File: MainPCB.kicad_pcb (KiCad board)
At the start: 4 copper layers, 105 x 62.4 mm, 41 parts, among them J1 RaspberryPi, J10 Conn_01x02, J2 Conn_01x03, J3 Screw_Terminal_01x02, J4 Conn_01x02, J5 Conn_01x06, J6 Conn_01x03_Pin, J7 Conn_01x10, J8 Conn_01x12, J9 Conn_01x04, M1 Motor_DC, M2 Motor_DC, M3 Motor_DC, M4 Motor_DC, SW1 SW_SPDT, SW2 SW_SPDT, SW3 SW_SPDT, SW4 SW_SPDT, SW5 SW_SPDT, SW6 SW_SPDT, SW7 SW_SPDT, U1 Teensy4.1, U10 Compass, U11 V_Regulator5v, U12 RockerSwitch, U13 V_Regulator3.3v, U2 VNH Driver, U3 VNH Driver, U4 VNH Driver, U5 VNH Driver, U6 TSOP25xx

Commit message: Finshined again
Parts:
- added J11: Conn_01x07, Connector_PinHeader_2.54mm:PinHeader_1x07_P2.54mm_Vertical, F.Cu at (117.9, 66.0)
- added R2: 10k, Capacitor_SMD:C_0805_2012Metric_Pad1.18x1.45mm_HandSolder, F.Cu at (139.4, 66.0)
- added R3: 10k, Capacitor_SMD:C_0805_2012Metric_Pad1.18x1.45mm_HandSolder, F.Cu at (142.4, 66.0)
- added R4: 10k, Capacitor_SMD:C_0805_2012Metric_Pad1.18x1.45mm_HandSolder, F.Cu at (145.4, 66.0)
- added R5: 10k, Capacitor_SMD:C_0805_2012Metric_Pad1.18x1.45mm_HandSolder, F.Cu at (148.4, 66.0)
- added R6: 10k, Capacitor_SMD:C_0805_2012Metric_Pad1.18x1.45mm_HandSolder, F.Cu at (151.5, 66.0)
- added R7: 10k, Capacitor_SMD:C_0805_2012Metric_Pad1.18x1.45mm_HandSolder, F.Cu at (154.5, 66.0)
- added R8: 10k, Capacitor_SMD:C_0805_2012Metric_Pad1.18x1.45mm_HandSolder, F.Cu at (157.5, 66.0)
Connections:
- J7 pad 1: 3.3V -> 5V
- U1 pad 23: STATE -> SLIDE1
- U1 pad 25: unconnected-(U1-33_MCLK2-Pad25) -> TRIG1
- U1 pad 26: SLIDE7 -> ECHO1
- U1 pad 27: SLIDE6 -> TRIG2
- U1 pad 28: SLIDE5 -> ECHO2
- U1 pad 29: SLIDE4 -> TRIG3
- U1 pad 30: SLIDE3 -> ECHO3
- U1 pad 31: SLIDE2 -> TRIG4
- U1 pad 32: SLIDE1 -> ECHO4
- U1 pad 46: 3.3V -> unconnected-(U1-3V3-Pad46)
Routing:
- net SLIDE1: track 59.7 -> 133.8 mm
- net 5V: track 168.1 -> 200.2 mm
- net SLIDE7: track 84.1 -> 116.1 mm, vias 1 -> 0
- net TRIG1: track 0.00 -> 31.7 mm
- net SLIDE6: track 79.1 -> 109.5 mm, vias 1 -> 0
- net ECHO1: track 0.00 -> 29.8 mm
- net TRIG3: track 0.00 -> 29.6 mm
- net ECHO2: track 0.00 -> 28.8 mm
- net ECHO3: track 0.00 -> 27.7 mm
- net TRIG2: track 0.00 -> 27.3 mm
- net ECHO4: track 0.00 -> 26.7 mm
- net STATE: track 26.6 -> 0.00 mm
- net SLIDE2: track 63.0 -> 89.3 mm
- net TRIG4: track 0.00 -> 25.2 mm
- net SLIDE4: track 72.0 -> 97.1 mm
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- removed copper zone on B.Cu, net GND
- removed copper zone on F.Cu, net GND
- removed copper zone on In1.Cu, net GND
- removed copper zone on In2.Cu, net GND

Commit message: finished final
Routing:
- added copper zone on B.Cu, net GND
- added copper zone on F.Cu, net GND
- added copper zone on In1.Cu, net GND
- added copper zone on In2.Cu, net GND
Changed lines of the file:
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@@
   (segment (start 190.5 91.704) (end 190.5 93.8755) (width 0.25) (layer "In2.Cu") (net 71))
   (segment (start 182.835 99.568) (end 181.3265 101.0765) (width 0.25) (layer "In2.Cu") (net 71))
+  (zone (net 1) (net_name "GND") (layers "F.Cu" "In1.Cu" "In2.Cu" "B.Cu") (hatch edge 0.5)
+    (connect_pads (clearance 0.5))
+    (min_thickness 0.25) (filled_areas_thickness no)
+    (fill yes (thermal_gap 0.5) (thermal_bridge_width 0.5) (island_removal_mode 1) (island_area_min 10))
+    (polygon
+      (pts
+        (xy 77.47 57.658)
+        (xy 74.676 128.524)
+        (xy 212.09 133.604)
+        (xy 205.232 54.356)
+      )
+    )
+  )
 )

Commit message: part movement
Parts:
- removed J11: Conn_01x07, Connector_PinHeader_2.54mm:PinHeader_1x07_P2.54mm_Vertical
- removed J7: Conn_01x10, Connector_IDC:IDC-Header_2x05_P2.54mm_Vertical
- removed R6, R7, R8: 10k, Capacitor_SMD:C_0805_2012Metric_Pad1.18x1.45mm_HandSolder
- removed SW5, SW6, SW7: SW_SPDT, SlideSW:SPDT_OS102011_CNK
- added J12: Conn_01x07, Connector_IDC:IDC-Header_2x04_P2.54mm_Vertical, F.Cu at (158.4, 111.7)
- H1, H2, H3, H4: footprint MountingHole:MountingHole_3.2mm_M3 -> MountingHole:MountingHole_3.2mm_M3_DIN965_Pad
- H5, H6, H7, H8: footprint MountingHole:MountingHole_2.7mm_M2.5 -> MountingHole:MountingHole_2.7mm_M2.5_DIN965_Pad
- J4, J8, M4: moved to F.Cu
- R2, R3, R4, R5: moved to B.Cu
- U10: footprint Connector_PinHeader_2.54mm:PinHeader_1x04_P2.54mm_Vertical -> Custom:Compass Sensor DFRobot
- U11, U13: footprint Connector_PinHeader_2.54mm:PinHeader_1x05_P2.54mm_Vertical -> Custom:Pololu Regulator
- moved U11 54.3 mm to (135.1, 116.4), turned to 90 degrees
- moved J2 51.5 mm to (189.0, 118.6)
- moved J9 39.5 mm to (189.4, 83.0), turned to -90 degrees
- moved J6 38.3 mm to (101.8, 72.4)
- moved R1 37.4 mm to (183.8, 91.3), turned to 90 degrees
- moved U6 36.2 mm to (158.2, 85.4)
- moved U10 32.2 mm to (160.8, 96.6)
- moved J10 29.3 mm to (175.3, 117.6), turned to 0 degrees
- moved D1 22.9 mm to (166.9, 85.4), turned to 180 degrees
- moved U1 19.5 mm to (118.8, 93.8)
- moved R5 19.0 mm to (137.6, 81.6)
- moved R2 17.2 mm to (146.6, 81.6)
- moved SW1 16.9 mm to (91.2, 105.8)
- moved SW2 16.9 mm to (91.2, 110.6)
- moved SW3 16.9 mm to (91.2, 115.5)
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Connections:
- U1 pad 26: ECHO1 -> ECHO
- U1 pad 28: ECHO2 -> SLIDE2
- U1 pad 30: ECHO3 -> SLIDE3
- U1 pad 32: ECHO4 -> SLIDE4
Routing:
- net GND: track 332.2 -> 0.00 mm
- net 12V: track 224.6 -> 0.00 mm
- net 5V: track 200.2 -> 0.00 mm
- net 3.3V: track 177.6 -> 0.00 mm
- net SLIDE1: track 133.8 -> 0.00 mm
- net SLIDE7: track 116.1 -> 0.00 mm
- net SLIDE6: track 109.5 -> 0.00 mm
- net SLIDE5: track 103.1 -> 0.00 mm
- net Net-(J3-Pin_2): track 100.2 -> 0.00 mm
- net RX4->TX: track 99.3 -> 0.00 mm
- net SLIDE4: track 97.1 -> 0.00 mm
- net TX4->RX: track 90.9 -> 0.00 mm
- net SLIDE2: track 89.3 -> 0.00 mm
- net SLIDE3: track 75.7 -> 0.00 mm, vias 1 -> 0
- net Kicker: track 67.8 -> 0.00 mm
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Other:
- outline, holes or cut-outs redrawn

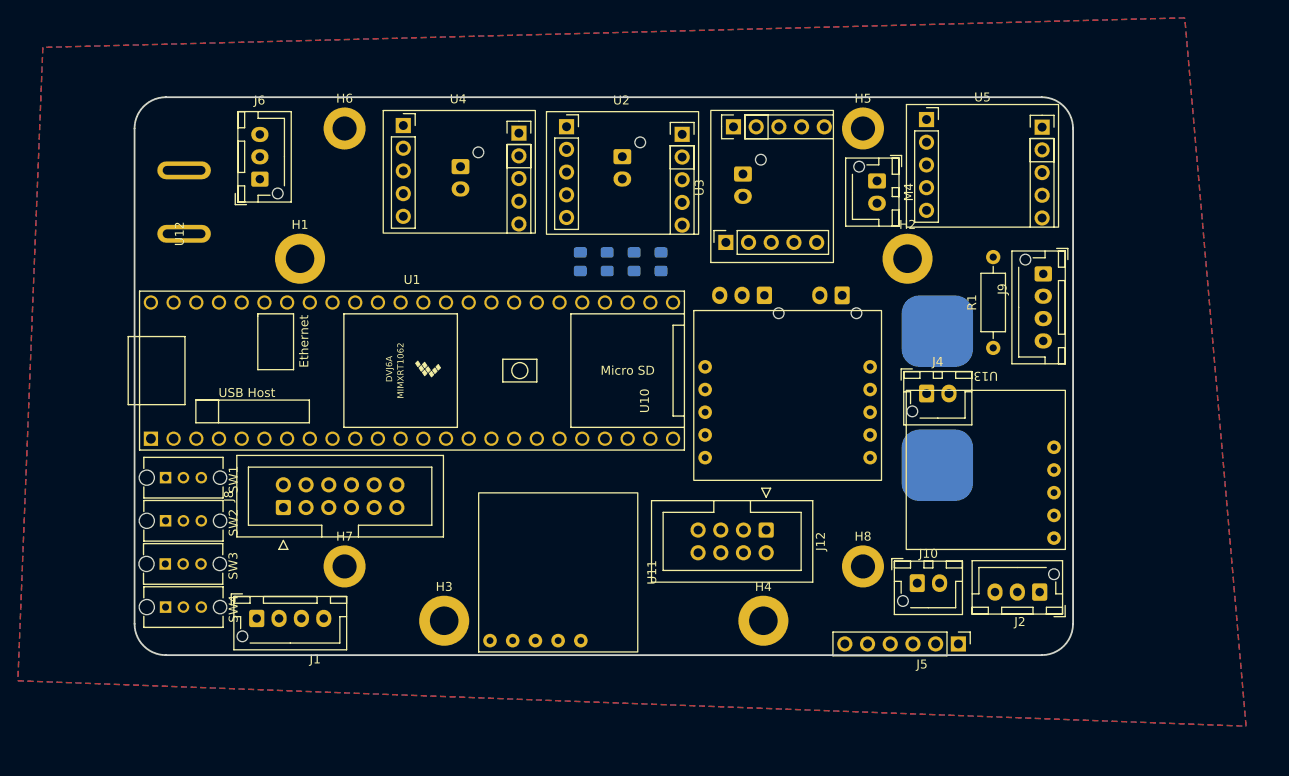
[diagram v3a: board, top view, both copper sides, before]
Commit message: Rerouted
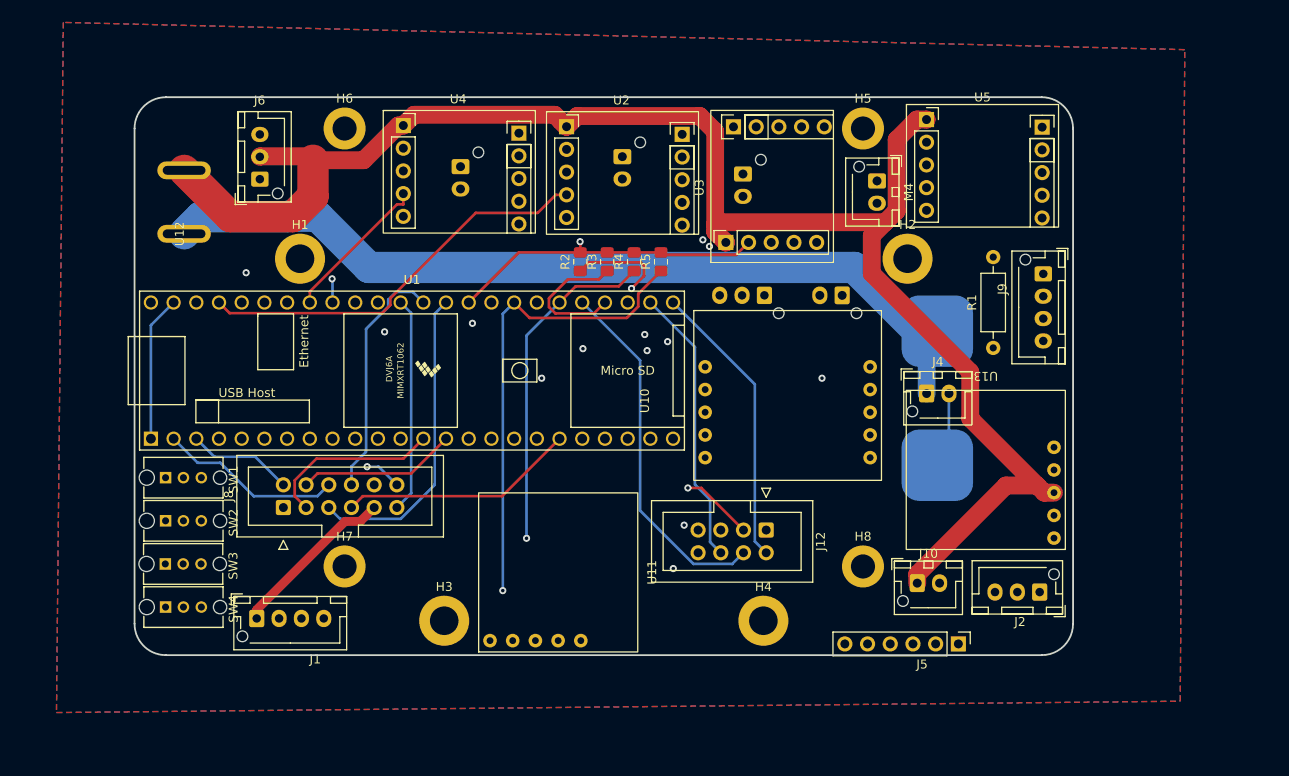
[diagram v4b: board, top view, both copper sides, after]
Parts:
- R2, R3, R4, R5: moved to F.Cu
- moved R2 9.03 mm to (137.6, 81.6)
- moved R5 9.03 mm to (146.6, 81.6)
- moved R3 3.01 mm to (140.6, 81.6)
- moved R4 3.01 mm to (143.6, 81.6)
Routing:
- net GND: track 0.00 -> 384.3 mm, vias 0 -> 1
- net 12V: track 0.00 -> 234.8 mm
- net 3.3V: track 0.00 -> 170.7 mm, vias 0 -> 1
- net 5V: track 0.00 -> 159.7 mm
- net Net-(J3-Pin_2): track 0.00 -> 97.9 mm
- net SLIDE4: track 0.00 -> 91.7 mm, vias 0 -> 1
- net SLIDE1: track 0.00 -> 90.1 mm, vias 0 -> 2
- net PWM4: track 0.00 -> 87.0 mm, vias 0 -> 2
- net ESC: track 0.00 -> 84.6 mm
- net DIR4A: track 0.00 -> 81.4 mm, vias 0 -> 2
- net SLIDE3: track 0.00 -> 79.6 mm, vias 0 -> 1
- net TX4->RX: track 0.00 -> 79.1 mm, vias 0 -> 1
- net SLIDE2: track 0.00 -> 77.5 mm, vias 0 -> 1
- net RX4->TX: track 0.00 -> 75.7 mm, vias 0 -> 1
- net PWM2: track 0.00 -> 74.1 mm
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
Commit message: Fixed Trace Widths
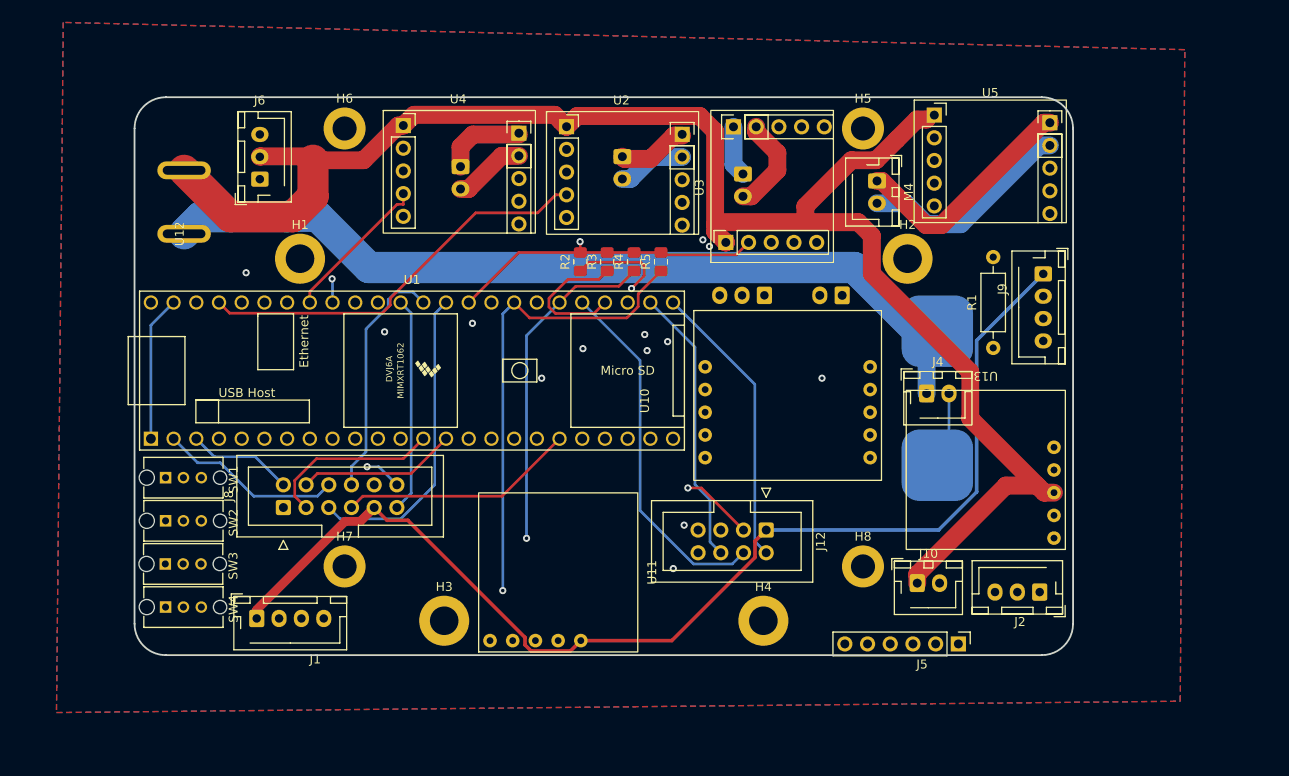
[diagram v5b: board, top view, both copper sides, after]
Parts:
- moved U5 1.00 mm to (183.3, 69.9)
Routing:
- net 5V: track 159.7 -> 174.7 mm
- net DIR4A: track 81.4 -> 94.3 mm
- net GND: track 384.3 -> 394.9 mm
- net Net-(M4-+): track 21.0 -> 26.1 mm
- net Net-(M4--): track 21.6 -> 24.0 mm
- net 12V: track 234.8 -> 237.1 mm
- net DIR1A: track 45.0 -> 46.1 mm
- net DIR4B: track 74.1 -> 75.2 mm
- net PWM4: track 87.0 -> 88.1 mm
- net Net-(M3-+): track 8.39 -> 9.32 mm
- net Net-(M2--): track 10.4 -> 10.9 mm

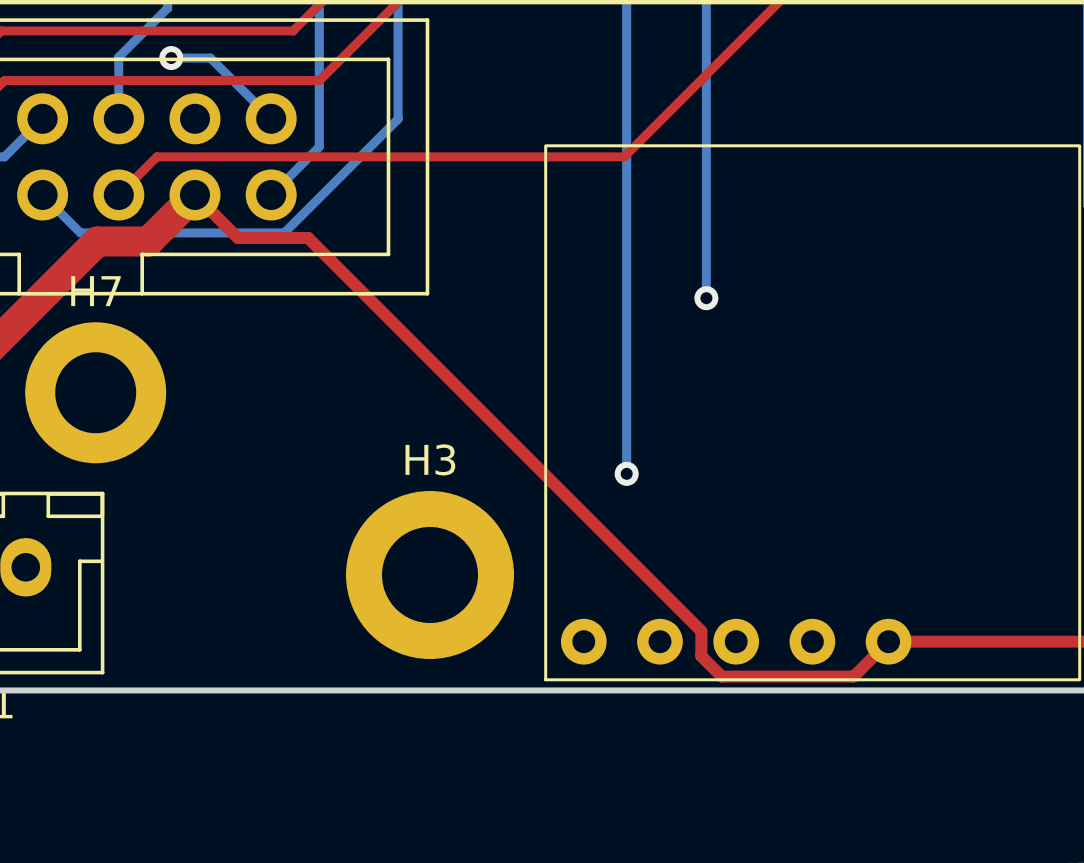
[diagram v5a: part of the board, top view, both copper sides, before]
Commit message: Fixed 5V trace
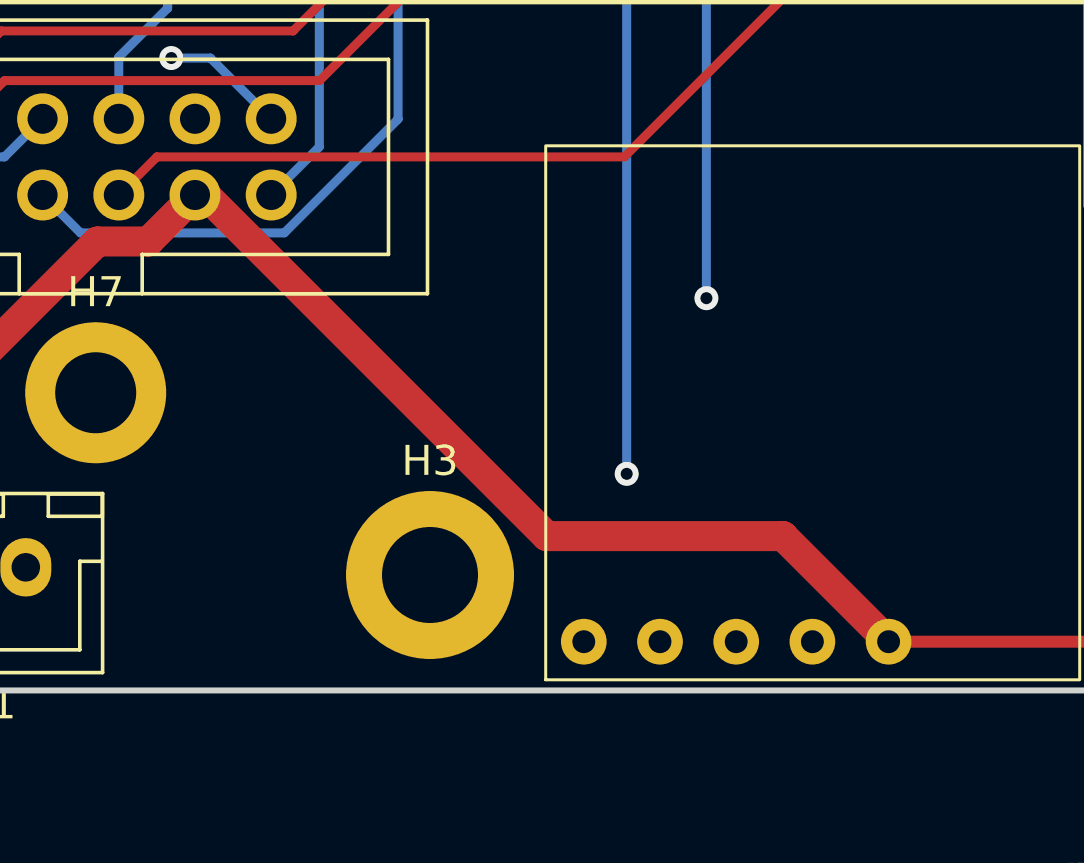
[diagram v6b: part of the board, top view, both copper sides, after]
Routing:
- net 5V: track 174.7 -> 173.2 mm
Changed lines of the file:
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@@
 	)
 	(segment
-		(start 132.098683 125.192)
-		(end 131.418 124.511317)
-		(width 0.4)
-		(layer "F.Cu")
-		(net 3)
-	)
-	(segment
 		(start 147.837767 124.03)
 		(end 157.15 114.717767)
@@
 	)
 	(segment
-		(start 115.97 110.57)
-		(end 114.54 109.14)
-		(width 0.4)
-		(layer "F.Cu")
-		(net 3)
-	)
-	(segment
-		(start 136.498 125.192)
-		(end 132.098683 125.192)
-		(width 0.4)
+		(start 134.14 120.51)
+		(end 137.66 124.03)
+		(width 1)
 		(layer "F.Cu")
 		(net 3)
@@
 	)
 	(segment
+		(start 114.887968 109.14)
+		(end 126.257968 120.51)
+		(width 1)
+		(layer "F.Cu")
+		(net 3)
+	)
+	(segment
 		(start 157.15 112.91)
 		(end 158.4 111.66)
@@
 	)
 	(segment
-		(start 131.418 124.511317)
-		(end 131.418 123.678)
-		(width 0.4)
-		(layer "F.Cu")
-		(net 3)
-	)
-	(segment
-		(start 118.31 110.57)
-		(end 115.97 110.57)
-		(width 0.4)
-		(layer "F.Cu")
-		(net 3)
-	)
-	(segment
-		(start 137.66 124.03)
-		(end 136.498 125.192)
-		(width 0.4)
+		(start 126.257968 120.51)
+		(end 134.14 120.51)
+		(width 1)
 		(layer "F.Cu")
 		(net 3)
 	)
 	(segment
-		(start 131.418 123.678)
-		(end 118.31 110.57)
-		(width 0.4)
+		(start 114.54 109.14)
+		(end 114.887968 109.14)
+		(width 1)
 		(layer "F.Cu")
 		(net 3)
@@
 	)
 	(segment
-		(start 169.527214 70.313)
-		(end 169.214214 70)
-		(width 0.3)
-		(layer "In1.Cu")
-		(net 54)
-	)
-	(segment
-		(start 164.2 71.02)
-		(end 164.2 77.936943)
+		(start 169.214214 70)
+		(end 165.806 70)
 		(width 0.3)
 		(layer "In1.Cu")
@@
 	)
 	(segment
-		(start 169.5 83.236943)
-		(end 169.5 88.9265)
+		(start 121.73 94.67)
+		(end 133.2803 94.67)
 		(width 0.3)
 		(layer "In1.Cu")
@@
 	)
 	(segment
-		(start 164.2 94.2265)
-		(end 164.6435 94.67)
+		(start 177.2075 70.313)
+		(end 169.527214 70.313)
 		(width 0.3)
 		(layer "In1.Cu")
@@
 	)
 	(segment
-		(start 177.2075 70.313)
-		(end 169.527214 70.313)
+		(start 164.2 71.02)
+		(end 164.2 77.936943)
 		(width 0.3)
 		(layer "In1.Cu")
@@
 	)
 	(segment
-		(start 121.73 94.67)
-		(end 133.2803 94.67)
+		(start 169.5 83.236943)
+		(end 169.5 89.8135)
 		(width 0.3)
 		(layer "In1.Cu")
@@
 	)
 	(segment
-		(start 169.214214 70)
-		(end 165.806 70)
+		(start 114.96 101.44)
+		(end 121.73 94.67)
 		(width 0.3)
 		(layer "In1.Cu")
@@
 	)
 	(segment
-		(start 169.5 88.9265)
-		(end 164.2 94.2265)
+		(start 165.806 70)
+		(end 165.493 70.313)
 		(width 0.3)
 		(layer "In1.Cu")
@@
 	)
 	(segment
-		(start 165.806 70)
-		(end 165.493 70.313)
+		(start 169.527214 70.313)
+		(end 169.214214 70)
 		(width 0.3)
 		(layer "In1.Cu")
@@
 	)
 	(segment
-		(start 114.96 101.44)
-		(end 121.73 94.67)
+		(start 169.5 89.8135)
+		(end 164.6435 94.67)
 		(width 0.3)
 		(layer "In1.Cu")

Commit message: Made Changes
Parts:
- H5, H6, H7, H8: footprint MountingHole:MountingHole_2.7mm_M2.5_DIN965_Pad -> MountingHole:MountingHole_3.2mm_M3_DIN965_Pad
- moved U11 12.6 mm to (126.1, 125.2), turned to 0 degrees
- moved M4 0.36 mm to (170.6, 72.9)
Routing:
- net GND: track 394.9 -> 398.8 mm
- net 12V: track 237.1 -> 240.5 mm
- net SLIDE4: track 91.7 -> 94.4 mm
- net 5V: track 173.2 -> 174.9 mm
- net 3.3V: track 170.7 -> 171.8 mm
- net DIR4A: track 93.9 -> 92.9 mm
- net TX2->RX: track 21.9 -> 22.9 mm

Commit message: fixed more errors
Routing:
- net 5V: track 174.9 -> 169.8 mm
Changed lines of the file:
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@@
 			)
 			(layer "F.CrtYd")
-			(net 165707684)
 		)
 		(fp_line
@@
 			)
 			(layer "F.CrtYd")
-			(net 165707684)
 		)
 		(fp_line
@@
 			(fill none)
 			(layer "F.SilkS")
-			(net 48)
 		)
 		(pad "1" thru_hole circle
@@
 	)
 	(segment
-		(start 101.4 121.55)
-		(end 101.4 116.427767)
-		(width 0.4)
-		(layer "In1.Cu")
-		(net 3)
-	)
-	(segment
 		(start 177.688114 111.66)
 		(end 158.4 111.66)
@@
 	)
 	(segment
-		(start 126.39 99.219755)
-		(end 126.39 102.35)
+		(start 126.46 100.358929)
+		(end 133.418929 93.4)
 		(width 0.4)
 		(layer "In2.Cu")
@@
 	)
 	(segment
-		(start 132.209755 93.4)
-		(end 126.39 99.219755)
+		(start 117.08 106.6)
+		(end 124.197057 106.6)
 		(width 0.4)
 		(layer "In2.Cu")
@@
 	)
 	(segment
-		(start 190.6 102.4)
-		(end 190.6 95.27573)
+		(start 124.197057 106.6)
+		(end 126.46 104.337057)
 		(width 0.4)
 		(layer "In2.Cu")
@@
 	)
 	(segment
-		(start 185.38427 90.06)
-		(end 154.91 90.06)
+		(start 190.6 96.1)
+		(end 190.6 102.4)
+		(width 0.4)
+		(layer "In2.Cu")
+		(net 6)
+	)
+	(segment
+		(start 151.57 93.4)
+		(end 154.89 90.08)
 		(width 0.4)
 		(layer "In2.Cu")
@@
 	)
 	(segment
-		(start 126.39 102.35)
-		(end 122.14 106.6)
+		(start 126.46 104.337057)
+		(end 126.46 100.358929)
 		(width 0.4)
 		(layer "In2.Cu")
@@
 	)
 	(segment
-		(start 122.14 106.6)
-		(end 117.08 106.6)
+		(start 133.418929 93.4)
+		(end 151.57 93.4)
 		(width 0.4)
 		(layer "In2.Cu")
@@
 	)
 	(segment
-		(start 190.6 95.27573)
-		(end 185.38427 90.06)
+		(start 154.89 90.08)
+		(end 184.58 90.08)
 		(width 0.4)
 		(layer "In2.Cu")
@@
 	)
 	(segment
-		(start 154.91 90.06)
-		(end 151.57 93.4)
-		(width 0.4)
-		(layer "In2.Cu")
-		(net 6)
-	)
-	(segment
-		(start 151.57 93.4)
-		(end 132.209755 93.4)
+		(start 184.58 90.08)
+		(end 190.6 96.1)
 		(width 0.4)
 		(layer "In2.Cu")
